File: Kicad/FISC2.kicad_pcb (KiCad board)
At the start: 2 copper layers, 214.6 x 123.2 mm, 73 parts, among them IC1 DS1233-10+, J1 Data Bus Pin Header, J2 Address Bus Pin Header, J3 uSeq Pin Header, J4 Control Lines Pin Header, J5 Spare Power Pins, J6 Clock Pin Header, SW1 SW_Push, U1 74HCT238, U10 74HCT574, U11 74HCT574, U12 74HCT541, U13 74HCT541, U14 74HCT574, U15 74HCT161, U16 AT27C1024-70PU, U17 74HCT151, U18 74HCT240, U19 74HCT154, U2 74HCT574, U20 74HCT154, U21 74HCT238, U22 74LS593, U23 74LS593, U24 74LS469, U25 74LS469, U26 74LS469, U27 74LS469, U28 74LS469, U29 74LS469, U3 CY62148, U4 AT28C64B, U5 74HCT139, U6 74HCT74, U7 74HCT574, U8 74HCT574, U9 M27C322-100F1

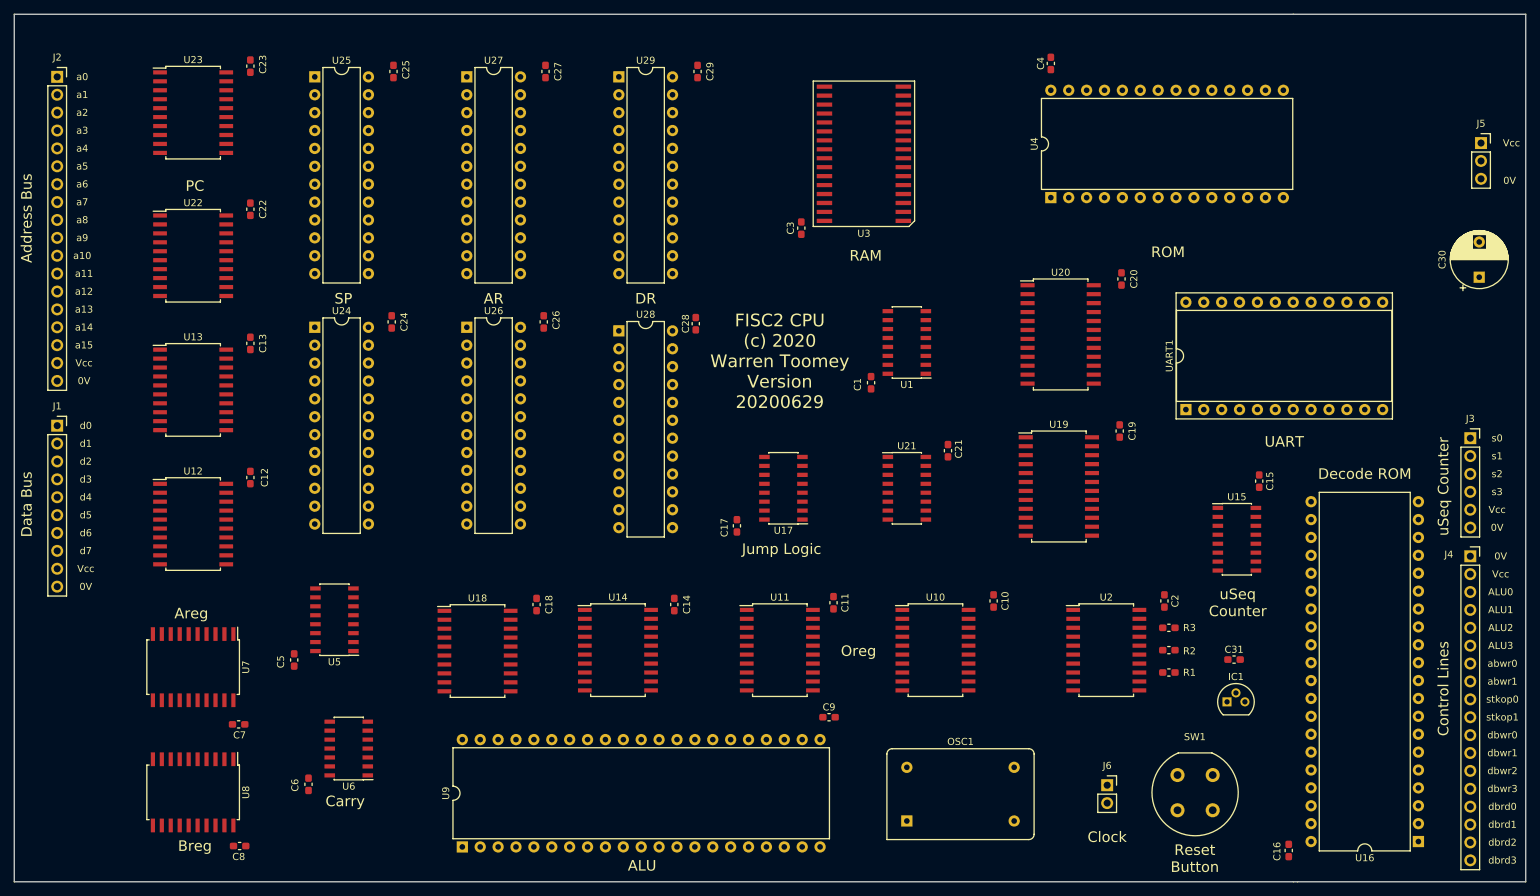
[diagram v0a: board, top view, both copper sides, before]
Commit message: More journal entries: testing the 22K pullups.
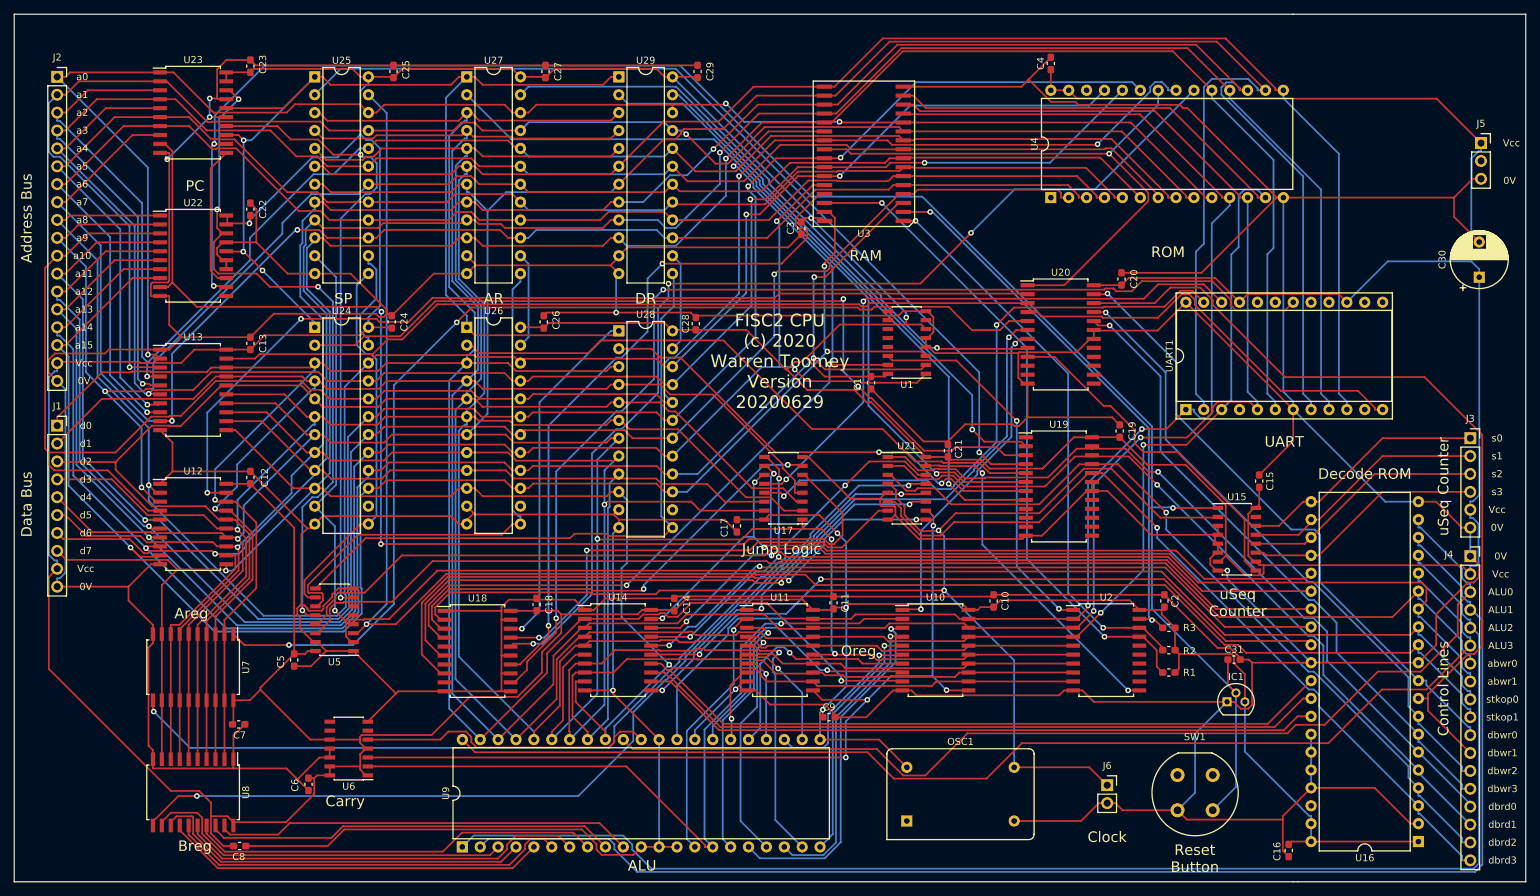
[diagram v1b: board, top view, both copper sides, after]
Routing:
- net Lo: track 0.00 -> 1528.9 mm, vias 0 -> 6
- net Hi: track 0.00 -> 1090.2 mm, vias 0 -> 6
- net NotZout: track 0.00 -> 552.5 mm, vias 0 -> 1
- net Zout: track 0.00 -> 551.7 mm, vias 0 -> 3
- net Nout: track 0.00 -> 542.6 mm, vias 0 -> 2
- net NorZout: track 0.00 -> 533.9 mm, vias 0 -> 4
- net ZNNout: track 0.00 -> 530.2 mm, vias 0 -> 3
- net NNNZout: track 0.00 -> 523.2 mm, vias 0 -> 2
- net d0: track 0.00 -> 516.3 mm, vias 0 -> 3
- net d7: track 0.00 -> 479.6 mm, vias 0 -> 3
- net adr11: track 0.00 -> 268.3 mm, vias 0 -> 3
- net adr10: track 0.00 -> 267.1 mm, vias 0 -> 2
- net adr8: track 0.00 -> 262.5 mm, vias 0 -> 3
- net ~Reset: track 0.00 -> 260.7 mm, vias 0 -> 3
- net StkOp1: track 0.00 -> 251.0 mm, vias 0 -> 1
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
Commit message: The PCB design is done, schematic updated, PCBs ordered.
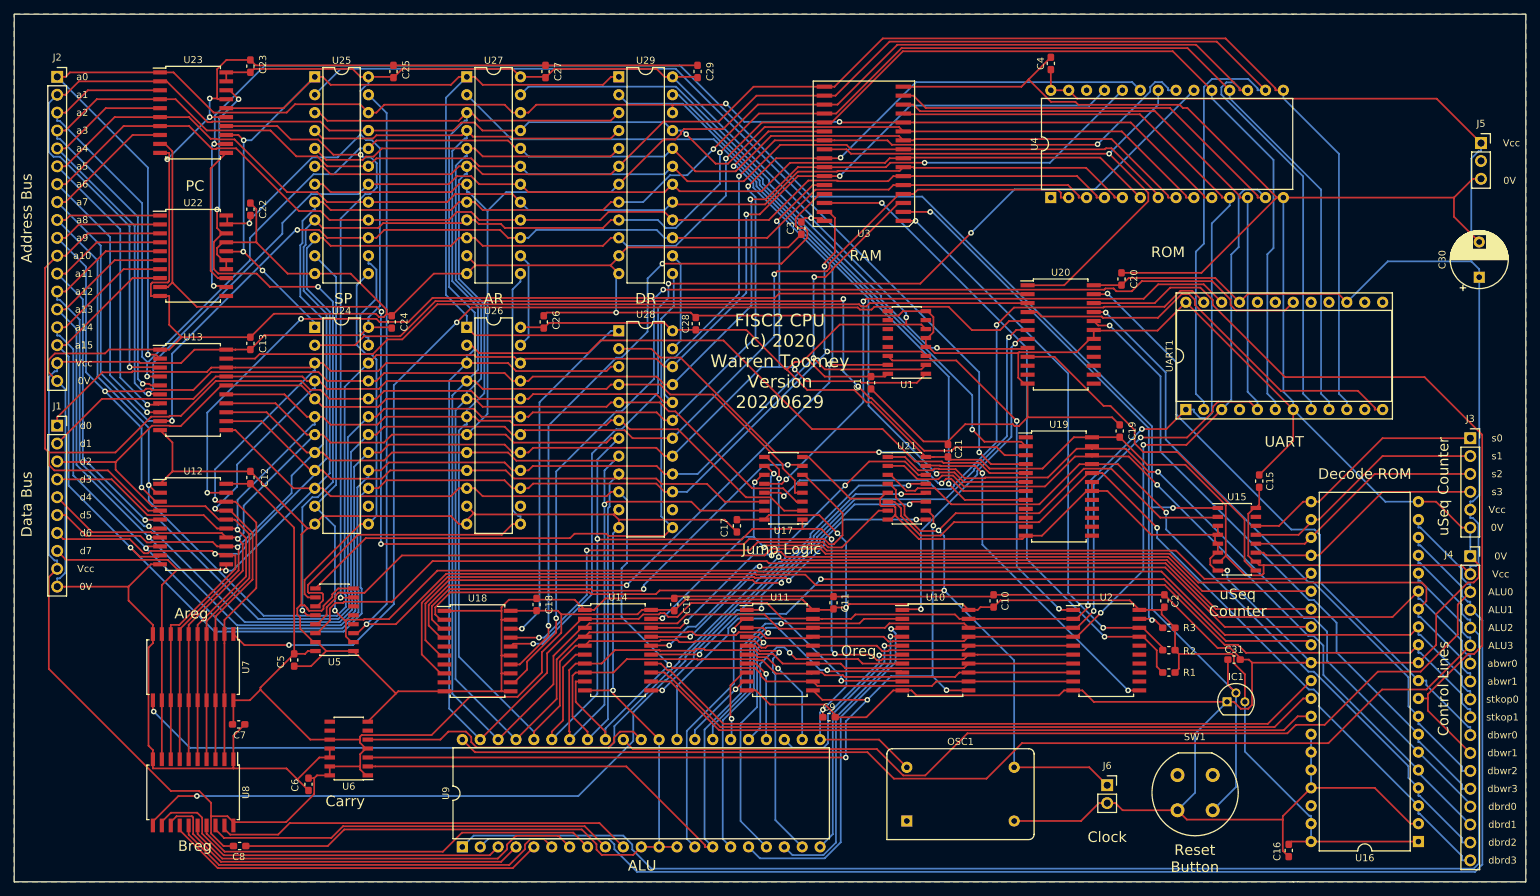
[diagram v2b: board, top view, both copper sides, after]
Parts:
- R1, R2, R3: value 1K -> 22K
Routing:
- added copper zone on B.Cu, net Lo
- added copper zone on F.Cu, net Lo
